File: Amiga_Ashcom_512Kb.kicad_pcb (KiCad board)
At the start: 2 copper layers, 87 x 48 mm, 23 parts, among them J1 PinSocket_2x28_P2.54mm_Horizo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, U1 74LS00N, U2 256kx4, U3 256kb x 4, U4 256kb x 4, U5 256kb x 4, U6 M6242B, Y9 32768Hz

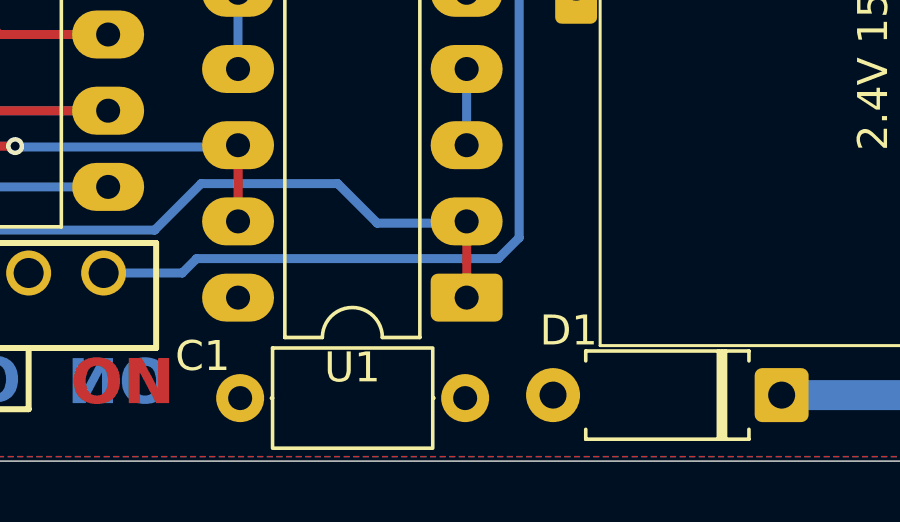
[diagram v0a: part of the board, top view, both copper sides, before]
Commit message: Annotated the schematic to match the PCB, and added experimental gerbers.
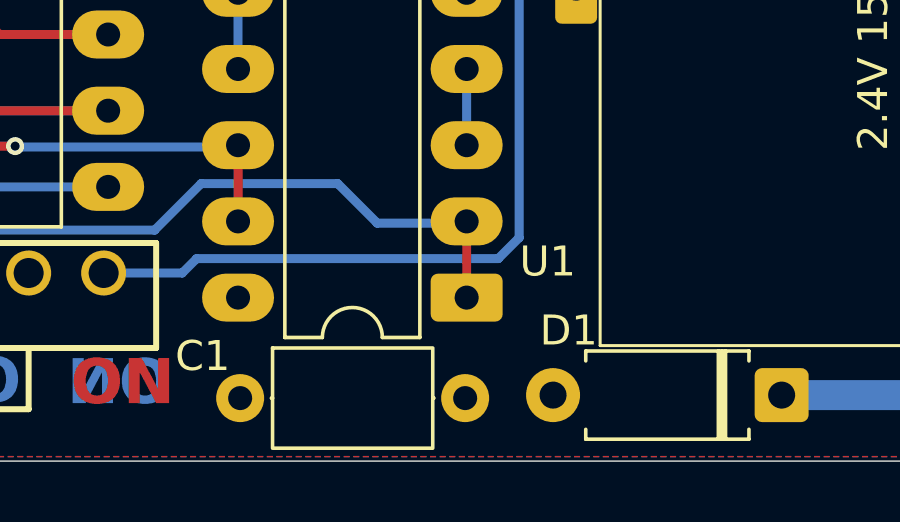
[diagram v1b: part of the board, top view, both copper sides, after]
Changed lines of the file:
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@@
 	)
 	(paper "A4")
+	(title_block
+		(title "Ashcom 512Kb Expansion for an Amiga 500")
+		(date "2025-07-23")
+		(rev "1")
+		(comment 1 "Reproduction of an Ashcom 512Kb Expansion card")
+	)
 	(layers
 		(0 "F.Cu" signal)
@@
 			(disableapertmacros no)
 			(usegerberextensions no)
-			(usegerberattributes yes)
-			(usegerberadvancedattributes yes)
-			(creategerberjobfile yes)
+			(usegerberattributes no)
+			(usegerberadvancedattributes no)
+			(creategerberjobfile no)
 			(dashed_line_dash_ratio 12.000000)
 			(dashed_line_gap_ratio 3.000000)
@@
 			(sketchdnponfab yes)
 			(crossoutdnponfab yes)
-			(subtractmaskfromsilk no)
+			(subtractmaskfromsilk yes)
 			(outputformat 1)
 			(mirror no)
-			(drillshape 1)
+			(drillshape 0)
 			(scaleselection 1)
-			(outputdirectory "")
+			(outputdirectory "production")
 		)
 	)
@@
 		(tags "THT DIP DIL PDIP 2.54mm 7.62mm 300mil LongPads")
 		(property "Reference" "U1"
-			(at 3.81 -2.33 0)
-			(layer "F.SilkS")
-			(effects
+			(at -2.7 1.2 0)
+			(layer "F.SilkS")
+			(effects

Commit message: Fix R1/R2 references and values, change C9 to 100nF
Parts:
- C9: value 22pF -> 100nF
- R1: value 47 -> 510
- U2: value 256kx4 -> 256kb x 4
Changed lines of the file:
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@@
 			)
 		)
-		(property "Value" "22pF"
+		(property "Value" "100nF"
 			(at 1.25 2.05 90)
 			(layer "F.Fab")
@@
 			)
 		)
-		(property "Value" "256kx4"
+		(property "Value" "256kb x 4"
 			(at 3.81 25.19 0)
 			(layer "F.Fab")
@@
 			)
 		)
-		(property "Value" "47"
+		(property "Value" "510"
 			(at 3.81 1.92 0)
 			(layer "F.Fab")

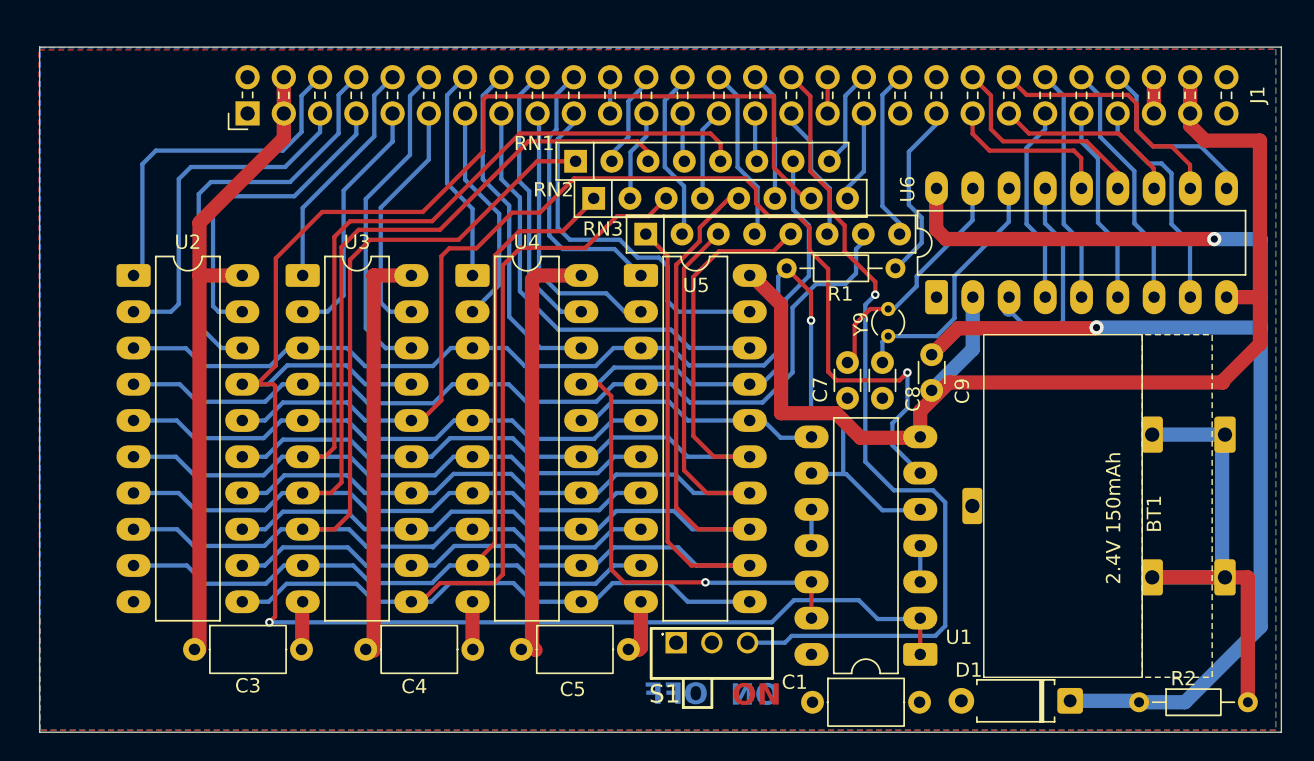
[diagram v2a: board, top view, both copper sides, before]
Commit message: Slightly increase width of board, move ON/OFF to correct layer, add additional info to silkscreen.
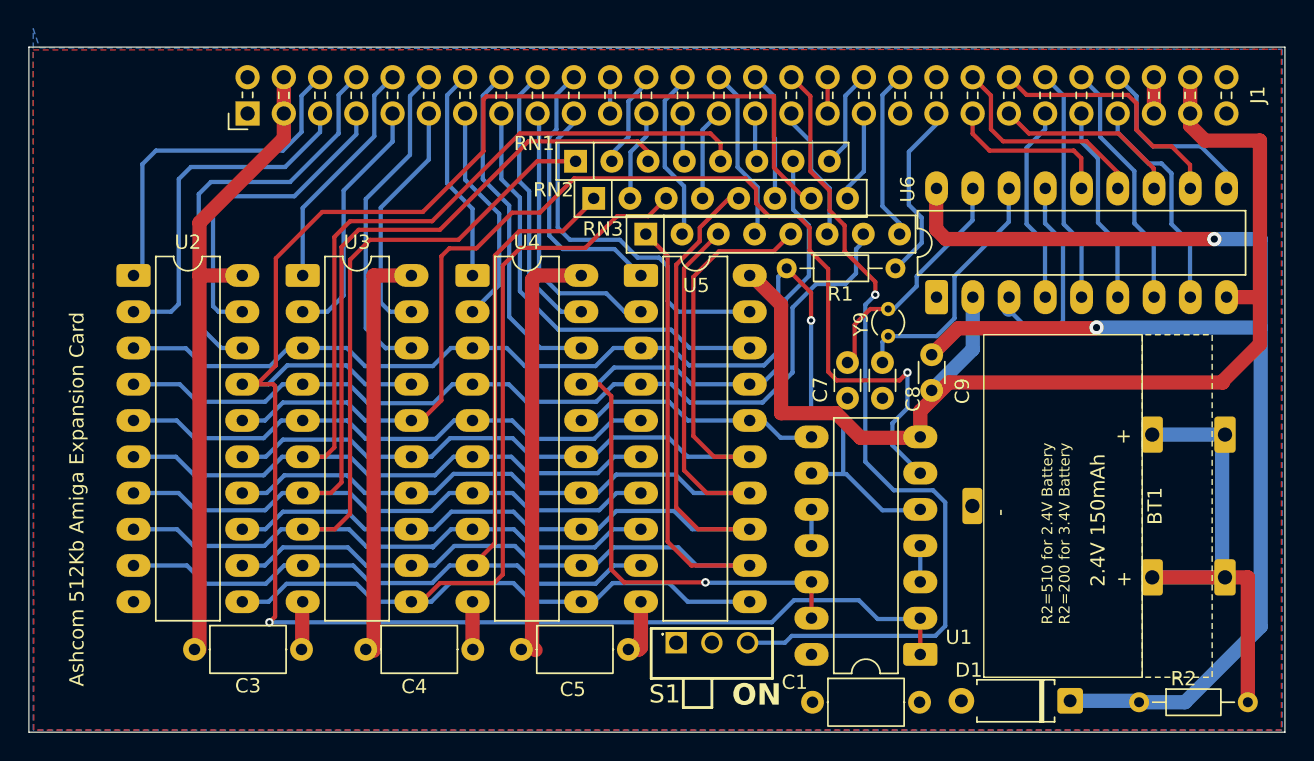
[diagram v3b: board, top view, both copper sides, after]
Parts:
- R1: value 510 -> 47
- R2: value 47 -> 510
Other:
- board size 87 x 48 mm -> 88 x 48 mm
- board text added: "+"
- board text added: "-"
- board text added: "Ashcom 512Kb Amiga Expansion Card"
- board text added: "Ashcom 512Kb Expansion Card. Recreated by CyberSwindy."
- board text added: "R2=510 for 2.4V Battery R2=200 for 3.4V Battery"
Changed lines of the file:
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@@
 		(at 144.1 90.65 90)
 		(property "Reference" "BT1"
-			(at -0.55 6.25 90)
+			(at 0 6.3 90)
 			(unlocked yes)
 			(layer "F.SilkS")
@@
 		)
 		(property "Value" "2.4V 150mAh"
-			(at -0.85 3.4 90)
+			(at -1 2.3 90)
 			(unlocked yes)
 			(layer "F.SilkS")
@@
 			)
 		)
-		(property "Value" "510"
+		(property "Value" "47"
 			(at 3.81 1.92 0)
 			(layer "F.Fab")
@@
 			)
 		)
-		(property "Value" "47"
+		(property "Value" "510"
 			(at 3.81 1.92 0)
 			(layer "F.Fab")
@@
 	)
 	(gr_rect
-		(start 72.25 58.5)
-		(end 159.25 106.5)
+		(start 71.5 58.5)
+		(end 159.5 106.5)
 		(stroke
 			(width 0.05)
@@
 		)
 	)
+	(gr_text "R2=510 for 2.4V Battery\nR2=200 for 3.4V Battery"
+		(at 144.5 98.95 90)
+		(layer "F.SilkS")
+		(effects
+			(font
+				(size 0.75 0.75)
+				(thickness 0.15)
+			)
+			(justify left bottom)
+		)
+	)
 	(gr_text "ON"
 		(at 120.75 104.75 0)
-		(layer "F.Cu")
+		(layer "F.SilkS")
 		(effects
 			(font
@@
 		)
 	)
-	(gr_text "OFF"
-		(at 119.1 104.7 0)
-		(layer "B.Cu")
+	(gr_text "+"
+		(at 148.75 86.35 90)
+		(layer "F.SilkS")
 		(effects
 			(font
-				(size 1.5 1.5)
-				(thickness 0.3)
-				(bold yes)
+				(size 1 1)
+				(thickness 0.15)
 			)
-			(justify left bottom mirror)
+			(justify left bottom)
 		)
 	)
-	(gr_text "ON"
-		(at 124.1 104.75 0)
-		(layer "B.Cu")
+	(gr_text "-"
+		(at 140.1 91.35 90)
+		(layer "F.SilkS")
+		(effects
+			(font
+				(size 1 1)
+				(thickness 0.15)
+			)
+			(justify left bottom)
+		)
+	)
+	(gr_text "Ashcom 512Kb Amiga Expansion Card"
+		(at 75.45 103.3 90)
+		(layer "F.SilkS")
+		(effects
+			(font
+				(size 1 1)
+				(thickness 0.15)
+			)
+			(justify left bottom)
+		)
+	)
+	(gr_text "+"
+		(at 148.8 96.35 90)
+		(layer "F.SilkS")
+		(effects
+			(font
+				(size 1 1)
+				(thickness 0.15)
+			)
+			(justify left bottom)
+		)
+	)
+	(gr_text "OFF"
+		(at 119.1 104.7 0)
+		(layer "B.SilkS")
 		(effects
 			(font
@@
 		)
 	)
-	(dimension
-		(type orthogonal)
-		(layer "User.1")
-		(pts
-			(xy 76 58.6) (xy 76.1 60.7)
-		)
-		(height -9.3)
-		(orientation 1)
-		(format
-			(prefix "")
-			(suffix "")
-			(units 3)
-			(units_format 0)
-			(precision 4)
-			(suppress_zeroes yes)
-		)
-		(style
-			(thickness 0.2)
-			(arrow_length 1.27)
-			(text_position_mode 2)
-			(arrow_direction outward)
-			(extension_height 0.58642)
-			(extension_offset 0.5)
-			(keep_text_aligned yes)
-		)
-		(gr_text "2.1"
-			(at 64.6 59.5 90)
-			(layer "User.1")
-			(effects
-				(font
-					(size 1.5 1.5)
-					(thickness 0.3)
-				)
+	(gr_text "ON"
+		(at 124.1 104.75 0)
+		(layer "B.SilkS")
+		(effects
+			(font
+				(size 1.5 1.5)
+				(thickness 0.3)
+				(bold yes)
 			)
+			(justify left bottom mirror)
 		)
 	)
-	(dimension
-		(type orthogonal)
-		(layer "User.1")
-		(pts
-			(xy 72.2 65.2) (xy 75.7 64.1)
-		)
-		(height -19.5)
-		(orientation 0)
-		(format
-			(prefix "")
-			(suffix "")
-			(units 3)
-			(units_format 0)
-			(precision 4)
-			(suppress_zeroes yes)
-		)
-		(style
-			(thickness 0.2)
-			(arrow_length 1.27)
-			(text_position_mode 0)
-			(arrow_direction outward)
-			(extension_height 0.58642)
-			(extension_offset 0.5)
-			(keep_text_aligned yes)
-		)
-		(gr_text "3.5"
-			(at 73.95 43.9 0)
-			(layer "User.1")
-			(effects
-				(font
-					(size 1.5 1.5)
-					(thickness 0.3)
-				)
+	(gr_text "Ashcom 512Kb Expansion Card. \nRecreated by CyberSwindy."
+		(at 76.45 73.2 90)
+		(layer "B.SilkS")
+		(effects
+			(font
+				(size 1 1)
+				(thickness 0.1)
 			)
+			(justify left bottom mirror)
 		)
 	)
@@
 		(layer "User.1")
 		(pts
-			(xy 159.25 60.6) (xy 155.4 60.8)
+			(xy 159.4 60.65) (xy 155.4 60.8)
 		)
 		(height -13.3)
@@
 			(keep_text_aligned yes)
 		)
-		(gr_text "3.85"
-			(at 157.325 45.5 0)
+		(gr_text "4"
+			(at 157.4 45.55 0)
 			(layer "User.1")
 			(effects
@@
 		(polygon
 			(pts
-				(xy 72.2 58.7) (xy 158.85 58.65) (xy 158.85 106.35) (xy 72.25 106.35)
+				(xy 71.79922 58.700231) (xy 159.25 58.649769) (xy 159.25 106.35) (xy 71.84922 106.35)
 			)
 		)
@@
 		(polygon
 			(pts
-				(xy 72.25 58.55) (xy 158.85 58.65) (xy 158.85 106.35) (xy 72.3 106.35) (xy 72.3 58.7)
+				(xy 72.25 58.55) (xy 159.3 58.650519) (xy 159.3 106.35) (xy 71.8 106.35) (xy 71.8 57.2)
 			)
 		)
